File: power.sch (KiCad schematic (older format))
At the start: 37 parts, among them J801 Conn_01x02, J802 Conn_01x02, Q801 DMMT5401, Q802 DMMT5401, U701 TPS61022, U702 TLV62585, U801 MCP73831-2-OT

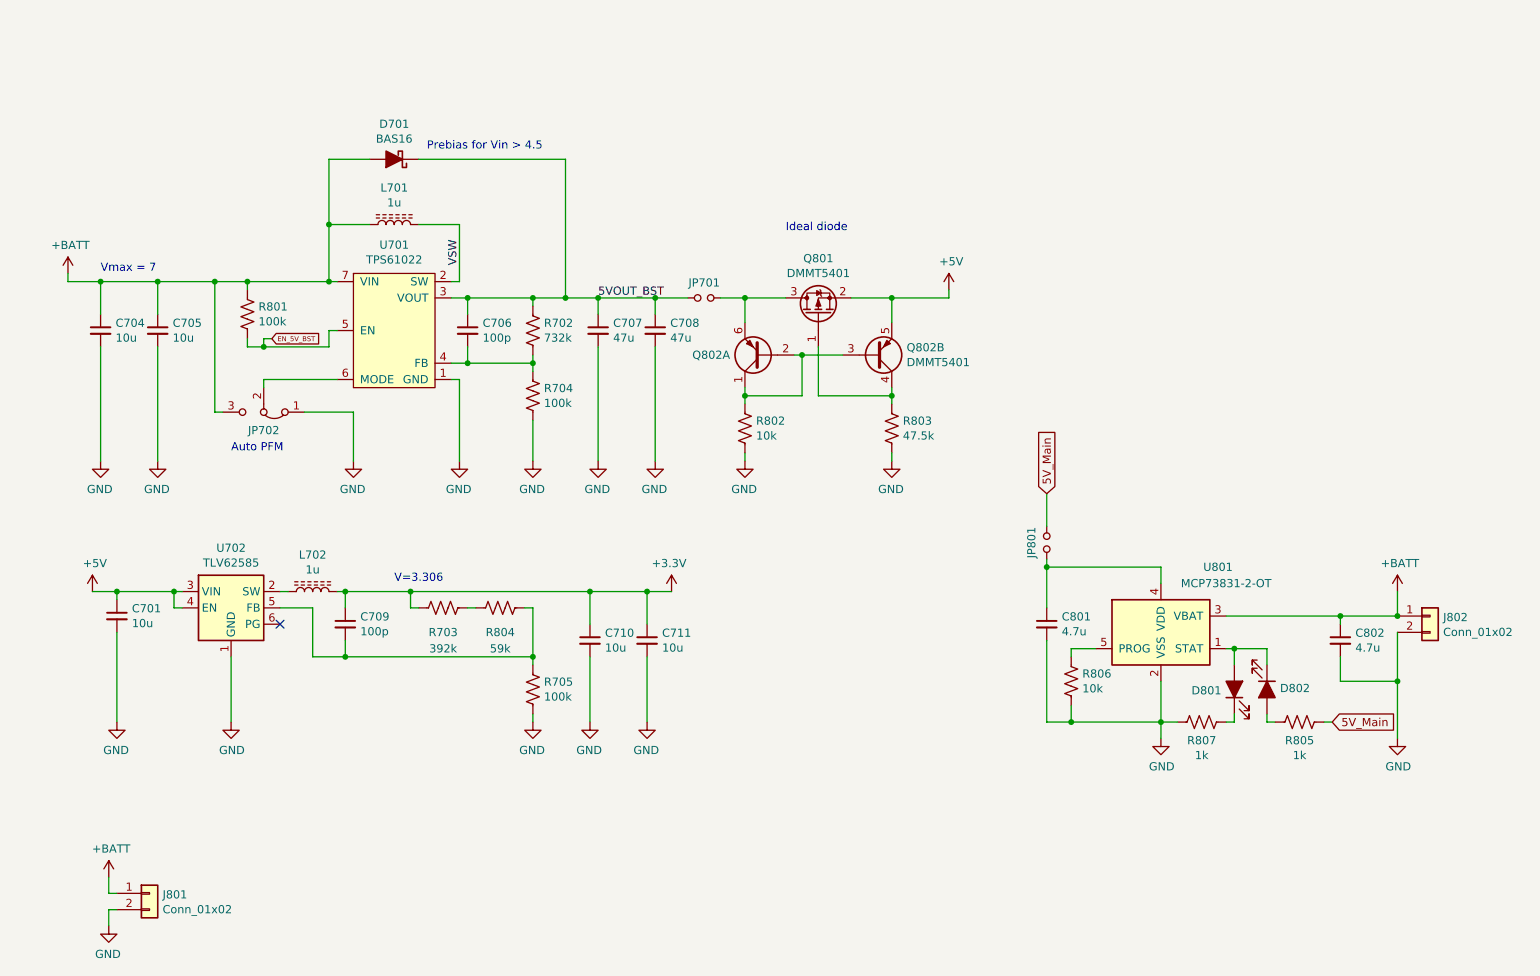
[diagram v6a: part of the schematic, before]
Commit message: Re-annotate all parts
Cleans up annotations
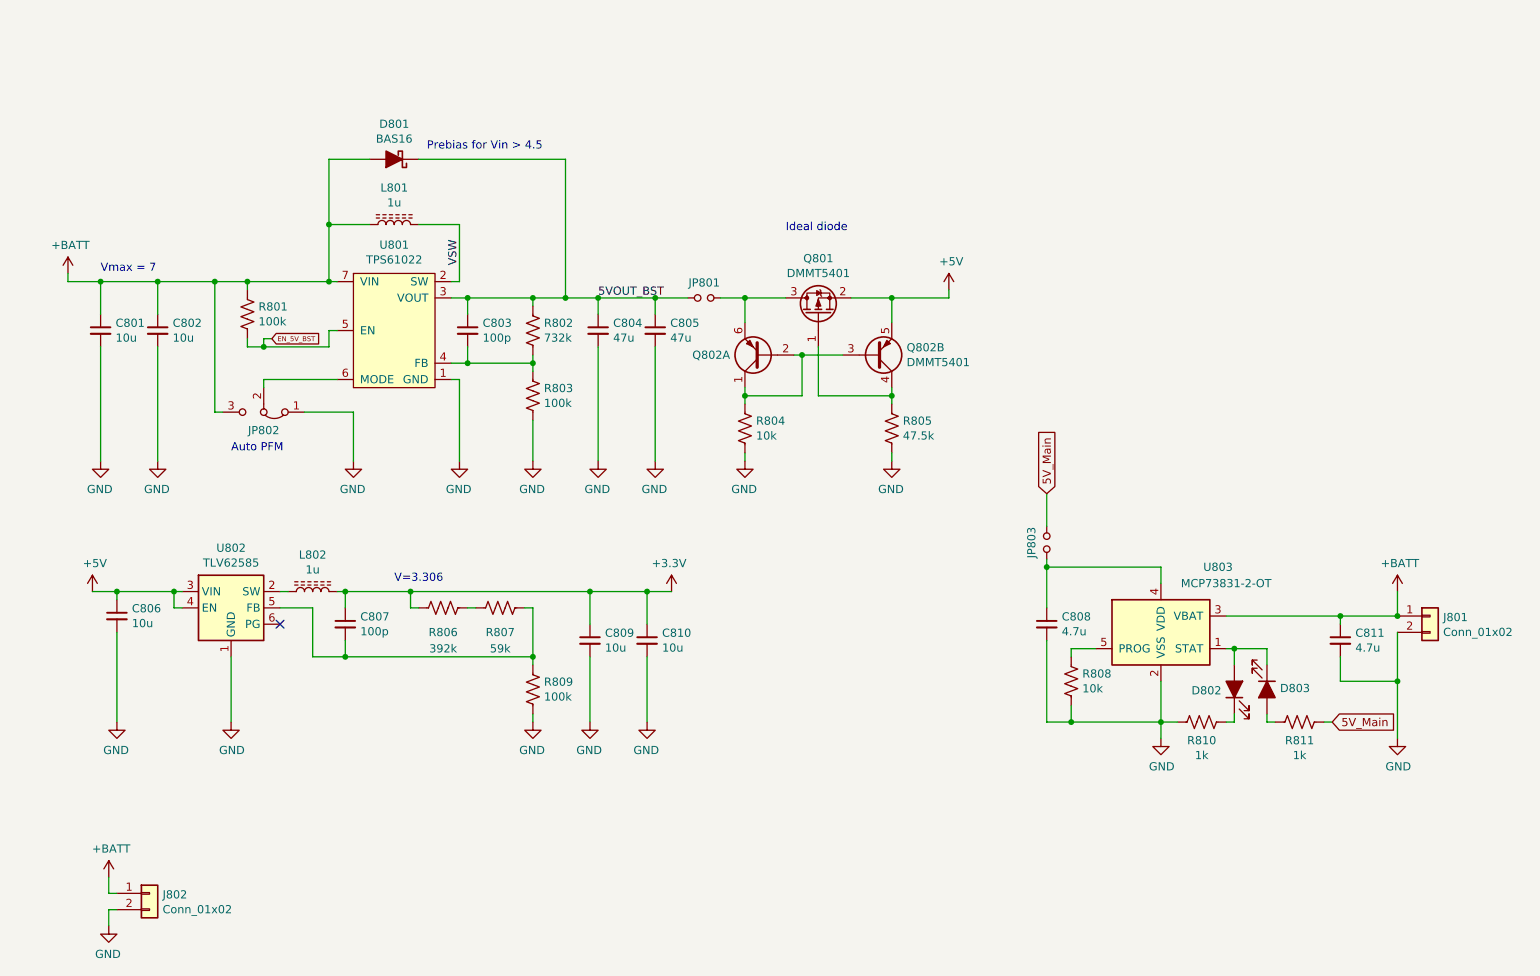
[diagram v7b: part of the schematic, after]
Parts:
- renumbered C704 to C801, C705 to C802, C706 to C803, C707 to C804, C708 to C805, C701 to C806, C709 to C807, C801 to C808, C710 to C809, C711 to C810, C802 to C811, D701 to D801, D801 to D802, D802 to D803, J802 to J801, J801 to J802, JP701 to JP801, JP702 to JP802, JP801 to JP803, L701 to L801, L702 to L802, R702 to R802, R704 to R803, R802 to R804, R803 to R805, R703 to R806, R804 to R807, R806 to R808, R705 to R809, R807 to R810, R805 to R811, U701 to U801, U702 to U802, U801 to U803

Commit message: Prefinal, layout done
Update FB to use inductor footprints
DNP net tie
Update diode symbol in power
Add battery voltage divider in power
Supply 5V power to aux sensor connector
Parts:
- added R812, R813: 10k, Resistor_SMD:R_0603_1608Metric, symbol Device:R_US
- D801: symbol Device:D_Schottky_ALT -> Device:D_ALT
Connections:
- net +BATT: now also R812.1
- net GND: now also R813.2
- new net BATT_Det: R812.2, R813.1
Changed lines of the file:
@@
 $EndComp
 $Comp
-L Device:D_Schottky_ALT D801
+L Device:D_ALT D801
 U 1 1 5E77A08E
 P 2950 1000
@@
 Wire Wire Line
 	2150 2150 2550 2150
+Text GLabel 10400 4150 0    50   Input ~ 0
+BATT_Det
+$Comp
+L Device:R_US R?
+U 1 1 5FD5B66D
+P 10450 4350
+AR Path="/5FD5B66D" Ref="R?"  Part="1"
+AR Path="/5FAF778C/5FD5B66D" Ref="R813"  Part="1"
+F 0 "R813" H 10518 4396 50  0000 L CNN
+F 1 "10k" H 10518 4305 50  0000 L CNN
+F 2 "Resistor_SMD:R_0603_1608Metric" H 10450 4350 60  0001 C CNN
+F 3 "" H 10450 4350 60  0001 C CNN
+F 4 "RC0603FR-0710KL" H 10450 4350 50  0001 C CNN "MPN"
+F 5 "311-10.0KHRCT-ND" H 10450 4350 50  0001 C CNN "Digikey"
+F 6 "RES SMD 10K OHM 1% 1/10W 0603" H 10450 4350 50  0001 C CNN "Note"
+	1    10450 4350
+	1    0    0    -1
+$EndComp
+$Comp
+L Device:R_US R?
+U 1 1 5FD5BDA6
+P 10450 3950
+AR Path="/5FD5BDA6" Ref="R?"  Part="1"
+AR Path="/5FAF778C/5FD5BDA6" Ref="R812"  Part="1"
+F 0 "R812" H 10518 3996 50  0000 L CNN
+F 1 "10k" H 10518 3905 50  0000 L CNN
+F 2 "Resistor_SMD:R_0603_1608Metric" H 10450 3950 60  0001 C CNN
+F 3 "" H 10450 3950 60  0001 C CNN
+F 4 "RC0603FR-0710KL" H 10450 3950 50  0001 C CNN "MPN"
+F 5 "311-10.0KHRCT-ND" H 10450 3950 50  0001 C CNN "Digikey"
+F 6 "RES SMD 10K OHM 1% 1/10W 0603" H 10450 3950 50  0001 C CNN "Note"
+	1    10450 3950
+	1    0    0    -1
+$EndComp
+Wire Wire Line
+	10400 4150 10450 4150
+Wire Wire Line
+	10450 4150 10450 4100
+Wire Wire Line
+	10450 4200 10450 4150
+Connection ~ 10450 4150
+$Comp
+L power:+BATT #PWR0145
+U 1 1 5FD74EBA
+P 10450 3750
+F 0 "#PWR0145" H 10450 3600 50  0001 C CNN
+F 1 "+BATT" H 10465 3923 50  0000 C CNN
+F 2 "" H 10450 3750 50  0001 C CNN
+F 3 "" H 10450 3750 50  0001 C CNN
+	1    10450 3750
+	1    0    0    -1
+$EndComp
+Wire Wire Line
+	10450 3800 10450 3750
+$Comp
+L power:GND #PWR0146
+U 1 1 5FD7A2ED
+P 10450 4550
+F 0 "#PWR0146" H 10450 4300 50  0001 C CNN
+F 1 "GND" H 10455 4377 50  0000 C CNN
+F 2 "" H 10450 4550 50  0001 C CNN
+F 3 "" H 10450 4550 50  0001 C CNN
+	1    10450 4550
+	1    0    0    -1
+$EndComp
+Wire Wire Line
+	10450 4550 10450 4500
 $EndSCHEMATC
